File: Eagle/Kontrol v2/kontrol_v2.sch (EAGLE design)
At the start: 21 parts, among them J1 1977477-2, X1 JST-XH-06-PIN-LONG-PAD, X10 JST-XH-02-PIN-LONG-PAD, X11 JST-XH-02-PIN-LONG-PAD, X12 JST-XH-02-PIN-LONG-PAD, X2 JST-XH-06-PIN-LONG-PAD, X3 JST-XH-04-PIN-LONG-PAD, X4 JST-XH-04-PIN-LONG-PAD, X5 JST-XH-04-PIN-LONG-PAD, X6 JST-XH-04-PIN-LONG-PAD, X8 JST-XH-03-PIN-LONG-PAD, X9 JST-XH-02-PIN-LONG-PAD

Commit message: edit kontrol v2
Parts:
- removed X2: JST-XH-06-PIN-LONG-PAD, JST XH Connectors v1-0:JST-XH-06-PIN-LONG-PAD
- removed X4: JST-XH-04-PIN-LONG-PAD, JST XH Connectors v1-0:JST-XH-04-PIN-LONG-PAD
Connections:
- removed net RX_TESTERBOARD: U$1.SD2
- removed net TEMP: X2-5.S
- removed net TX_TESTERBOARD: U$1.SD3
- new net 5V_ESP: U$1.5V
- new net CUR_SENSE: X3-3.S
- new net PWM_DISCHARGE: X1-4.S
- new net PWM_MOSFET: X1-3.S
- new net VOL_SENSE: X3-4.S
- net 12V: no longer X2-1.S
- net 5V: no longer U$1.5V, X2-2.S, X4-1.S
- net CUR_SENSE_1: no longer X3-3.S
- net CUR_SENSE_2: no longer X4-3.S
- net GND: no longer X2-6.S, X4-2.S
- net PWM_DISCHARGE_KANAN: no longer X2-4.S
- net PWM_DISCHARGE_KIRI: no longer X1-4.S
- net PWM_MOSFET_KANAN: no longer X2-3.S
- net PWM_MOSFET_KIRI: no longer X1-3.S
- net VOL_SENSE_1: no longer X3-4.S
- net VOL_SENSE_2: no longer X4-4.S

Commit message: nambahin library eagle+update kontrolv2
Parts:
- removed J1: 1977477-2, terminal_block:1977477-2
- removed JP1: (no value), pinhead:PINHD-1X7
- removed JP5: (no value), pinhead:PINHD-1X10
- added 1K: 1k, rcl:R-US_0204/7
- added 330: 6k, rcl:R-US_0204/7
- added C3: (no value), rcl:CPOL-EUE2,5-6E
- added D4: (no value), Sparkfun_LED:LED5MM
- added D7: UF4007, diode:BAS15
- added JP3: (no value), pinhead:PINHD-1X16
- added JP6: (no value), pinhead:PINHD-1X9
- added JP7: (no value), pinhead:PINHD-1X2
- added JP8: (no value), pinhead:PINHD-1X1
- added K1: SRD-12VDC-SL-C, TA_library:SRD-12VDC-SL-C
- added NPN: (no value), transistor:BC547A-NPN-TO92-CBE
- added U$2: ADS1115, ADS1115:ADS1115
- added U$3: SIM800V2, sim800v2:SIM800V2
- added X2: JST-XH-03-PIN-LONG-PAD, JST XH Connectors v1-0:JST-XH-03-PIN-LONG-PAD
- JP4: device pinhead:PINHD-1X10 -> pinhead:PINHD-1X1
- renumbered X9 to OVR_BMS
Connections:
- removed net CUR_SENSE_1: JP5.7
- removed net CUR_SENSE_2: JP5.9
- removed net N$10: X10-2.S
- removed net N$12: X11-2.S
- removed net N$14: X12-2.S
- removed net N$2: HI_LINK1.AC-, J1.1
- removed net N$3: U$1.IO13
- removed net N$43: JP4.6
- removed net N$46: JP4.9
- removed net N$47: JP4.10
- removed net N$53: JP5.6
- removed net N$7: OVR_BMS-2.S
- removed net PWM_DISCHARGE_KANAN: U$1.IO23
- removed net PWM_DISCHARGE_KIRI: U$1.IO18
- removed net PWM_MOSFET_KANAN: U$1.IO19
- removed net PWM_MOSFET_KIRI: U$1.IO17
- removed net TEMP2: JP4.8
- removed net VOL_SENSE_1: JP5.8
- removed net VOL_SENSE_2: JP5.10
- new net AC: K1.COM
- new net AC_IN_1: K1.NO
- new net EN: C3.+, U$1.EN
- new net N$19: 1K.2, NPN.B
- new net N$21: D7.A, K1.COIL2, NPN.C
- new net N$23: JP3.14, U$1.IO0
- new net N$24: JP3.15, U$1.IO2
- new net N$44: JP8.1, U$2.A3
- new net N$9: JP6.3, U$1.IO12
- new net RELAY: 1K.1, D4.C, JP6.7, U$1.IO25
- new net RX_BMS: JP3.4, U$1.TXD0
- new net RX_IOT: JP6.6, U$1.IO26
- new net TEMP: U$2.A2, X2-2.S
- new net TX_BMS: JP3.5, U$1.RXD0
- new net TX_IOT: JP6.5, U$1.IO27
- net 12V: now also JP4.1
- net 5V: now also D7.C, JP7.1, K1.COIL1, U$2.5V, U$3.5V, X2-1.S; no longer JP1.7, JP4.1, JP5.1, JP5.5
- net 5V_ESP: now also JP7.2
- net BLU_KANAN: now also JP3.9, U$1.IO18; no longer U$1.IO5
- net BLU_KIRI: now also JP3.13, U$1.IO4; no longer U$1.IO0
- net CUR_SENSE: now also U$2.A0
- net DETEKSI_BATERAI_KANAN: now also JP6.8
- net DETEKSI_BATERAI_KIRI: now also JP6.9, U$1.IO32; no longer U$1.IO26
- net GND: now also 330.1, C3.-, JP3.1, JP3.7, NPN.E, OVR_BMS-2.S, U$2.ADDR, U$2.GND, U$3.GND, U$3.GND\, X10-2.S, X11-2.S, X12-2.S, X2-3.S; no longer JP1.6, JP4.2, JP4.5, JP5.2
- net GRN_KANAN: now also JP3.2, U$1.IO23; no longer U$1.IO16
- net GRN_KIRI: now also JP3.11, U$1.IO17; no longer U$1.IO2
- net N$1: now also 330.2, D4.A; no longer HI_LINK1.AC+, J1.2
- net N$8: now also JP6.2, U$1.GND@14; no longer U$1.IO32
- net OVERRIDE_BMS: now also JP6.1, U$1.IO13; no longer U$1.IO27
- net PWM_DISCHARGE: now also JP3.16, U$1.IO15
- net PWM_MOSFET: now also JP3.10, U$1.IO5
- net RED_KANAN: now also JP3.8, U$1.IO19; no longer U$1.IO4
- net RED_KIRI: now also JP3.12, U$1.IO16; no longer U$1.IO15
- net RX: now also U$3.RX; no longer JP1.4, U$1.RXD0
- net SCL: now also JP3.3, U$2.SCL; no longer JP4.3, JP5.3
- net SDA: now also JP3.6, U$2.SDA; no longer JP4.4, JP5.4
- net SWITCH_MODE_DAYA: now also JP6.4, U$1.IO14; no longer U$1.IO25
- net TEMP1: no longer JP4.7
- net TX: now also U$3.TX; no longer JP1.3, U$1.TXD0
- net VOL_SENSE: now also U$2.A1
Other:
- note removed: "RST GND RX TX VDD GND 5V"
- moved on the sheet: X1-1, X1-2, X1-3, X1-4, X1-5, X1-6

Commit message: Update board kontrol
Harusnya sudah selesai
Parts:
- removed X1: JST-XH-06-PIN-LONG-PAD, JST XH Connectors v1-0:JST-XH-06-PIN-LONG-PAD
- removed X5, X6: JST-XH-04-PIN-LONG-PAD, JST XH Connectors v1-0:JST-XH-04-PIN-LONG-PAD
- added 5V: 5V, pinhead:PINHD-1X5
- added C5: 2mF, rcl:CPOL-EUE3.5-10
- added CHARGER: JST-XH-08-PIN-LONG-PAD, Rembrandt Electronics - JST XH Connectors v1-0:JST-XH-08-PIN-LONG-PAD
- added GND: GND, pinhead:PINHD-1X5
- added LED_L, LED_R: JST-XH-04-PIN-LONG-PAD, JST XH Connectors v1-0:JST-XH-04-PIN-LONG-PAD
- added U$4: TERMINAL_4P, TA_library:TERMINAL_4P
- C1: value (none) -> 22u
- C2: value (none) -> 100n
- C3: value (none) -> 4.7uF
- D4: value (none) -> LED_G
- NPN: value (none) -> BS170
- renumbered X10 to CHGMODE, X11 to DB_L, X12 to DB_R, X2 to TEMP, X3 to SENSING, X8 to FAN
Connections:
- removed net AC: K1.COM
- removed net AC_IN_1: K1.NO
- removed net CUR_SENSE: SENSING-3.S, U$2.A0
- removed net N$4: JP2.1
- removed net N$5: JP2.3
- removed net N$6: JP2.5
- removed net RX: U$3.RX
- removed net TEMP: TEMP-2.S, U$2.A2
- removed net TEMP1: X1-5.S
- removed net TX: U$3.TX
- removed net VOL_SENSE: SENSING-4.S, U$2.A1
- new net AC+: HI_LINK1.AC+, U$4.IN_2, U$4.IN_3
- new net AC-: HI_LINK1.AC-, K1.COM, U$4.IN_1
- new net AC_OUT_CHG: K1.NO, U$4.IN_4
- new net CURRENT_SENSE: CHARGER-6.S, SENSING-3.S, U$2.A0
- new net N$2: FAN-1.S
- new net TEMP_SENSE: CHARGER-5.S, TEMP-2.S, U$2.A2
- new net VOLTAGE_SENSE: CHARGER-7.S, SENSING-4.S, U$2.A1
- net 12V: now also CHARGER-1.S; no longer X1-1.S
- net 5V: now also 5V.1, 5V.2, 5V.3, 5V.4, 5V.5, C5.+, CHARGER-2.S; no longer X1-2.S
- net BLU_KANAN: now also LED_R-3.S; no longer X6-2.S
- net BLU_KIRI: now also LED_L-3.S; no longer X5-2.S
- net GND: now also C5.-, CHARGER-8.S, GND.1, GND.2, GND.3, GND.4, GND.5, JP2.5, LED_L-4.S, LED_R-4.S; no longer JP3.1, U$1.GND@38, X1-6.S, X5-1.S, X6-1.S
- net GRN_KANAN: now also LED_R-1.S; no longer X6-4.S
- net GRN_KIRI: now also LED_L-1.S; no longer X5-4.S
- net PWM_DISCHARGE: now also CHARGER-4.S; no longer X1-4.S
- net PWM_MOSFET: now also CHARGER-3.S; no longer X1-3.S
- net RED_KANAN: now also LED_R-2.S; no longer X6-3.S
- net RED_KIRI: now also LED_L-2.S; no longer X5-3.S
- net RX_BMS: now also JP2.1
- net RX_IOT: now also U$3.RX
- net TX_BMS: now also JP2.3
- net TX_IOT: now also U$3.TX
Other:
- moved on the sheet: 1K, 330, D7, JP6, NPN

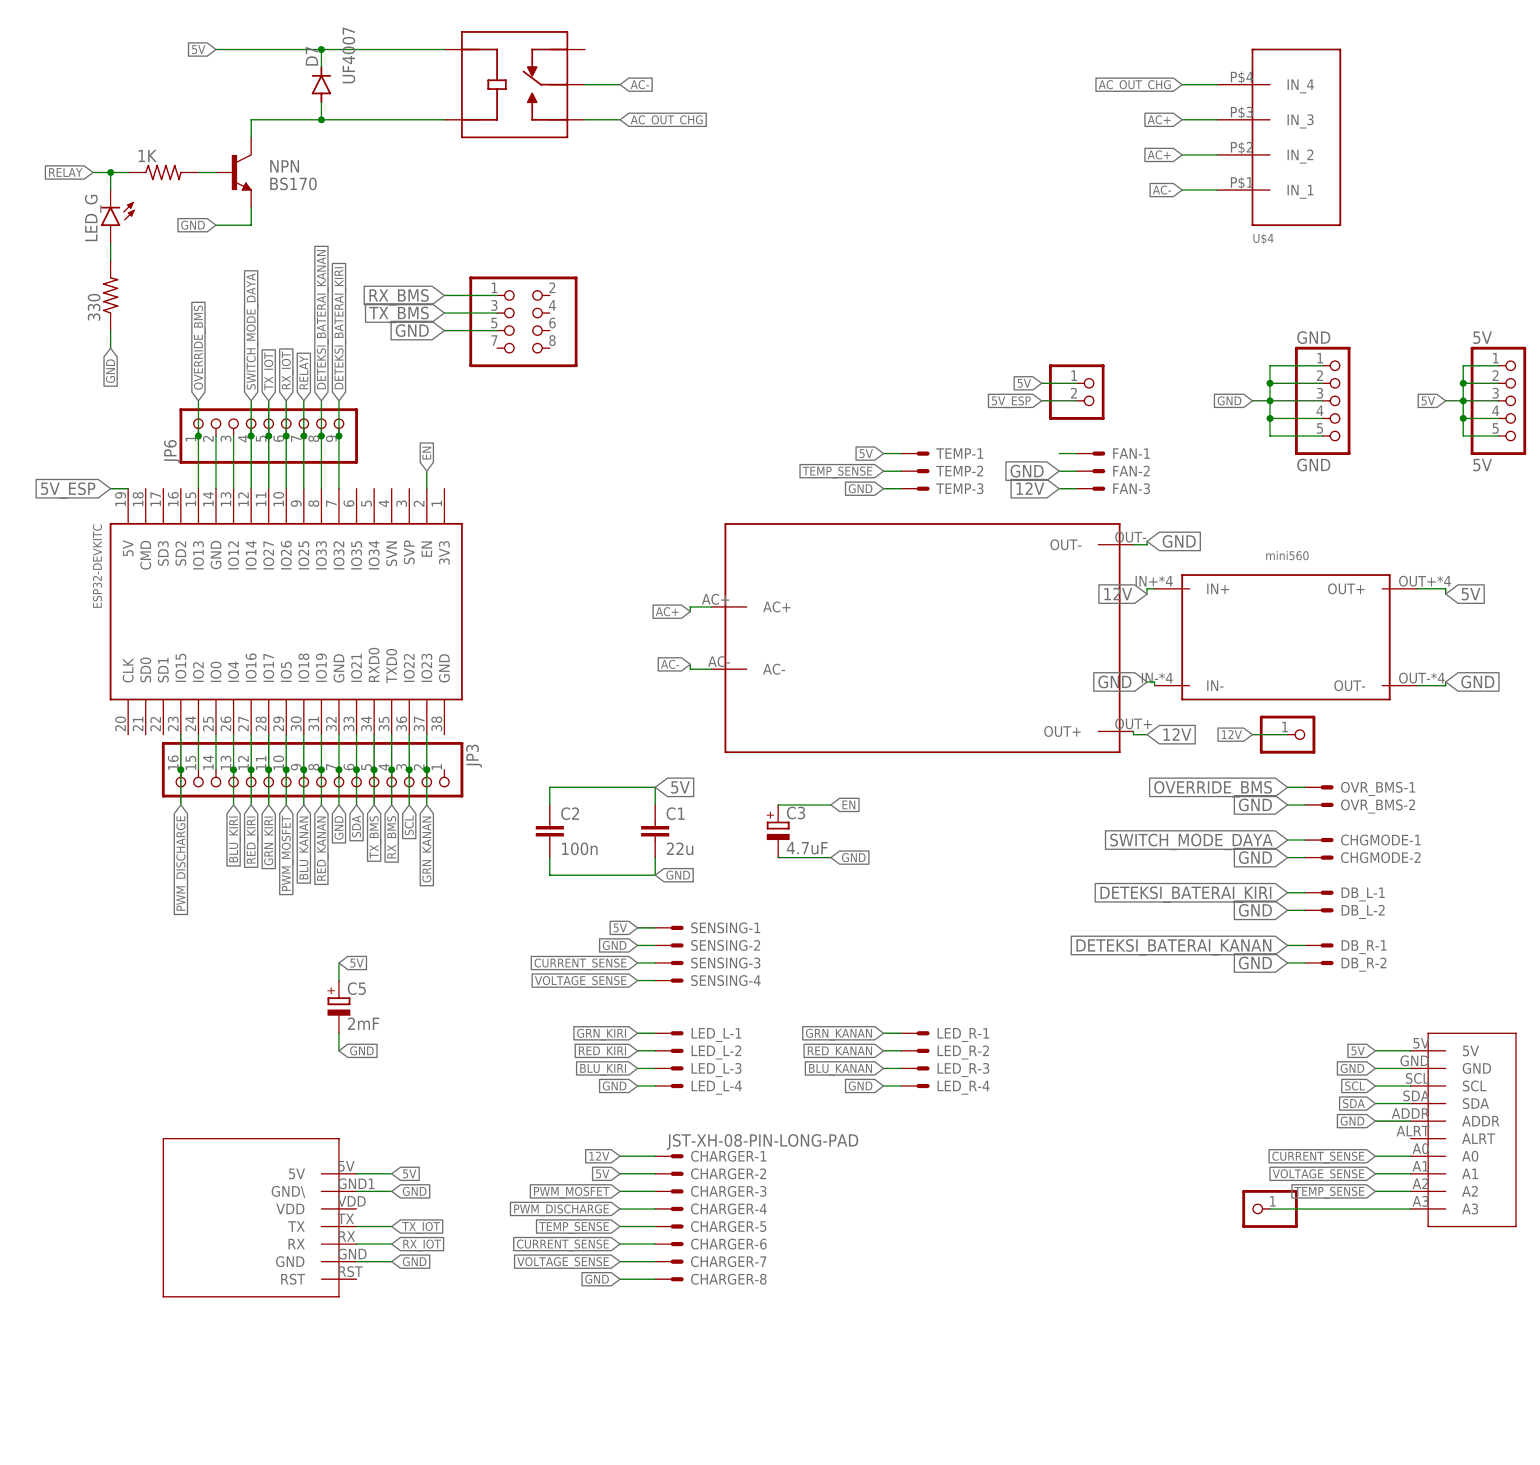
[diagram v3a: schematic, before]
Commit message: Update kontrol
XH8 -> xh10
4p term -> 2p term x2
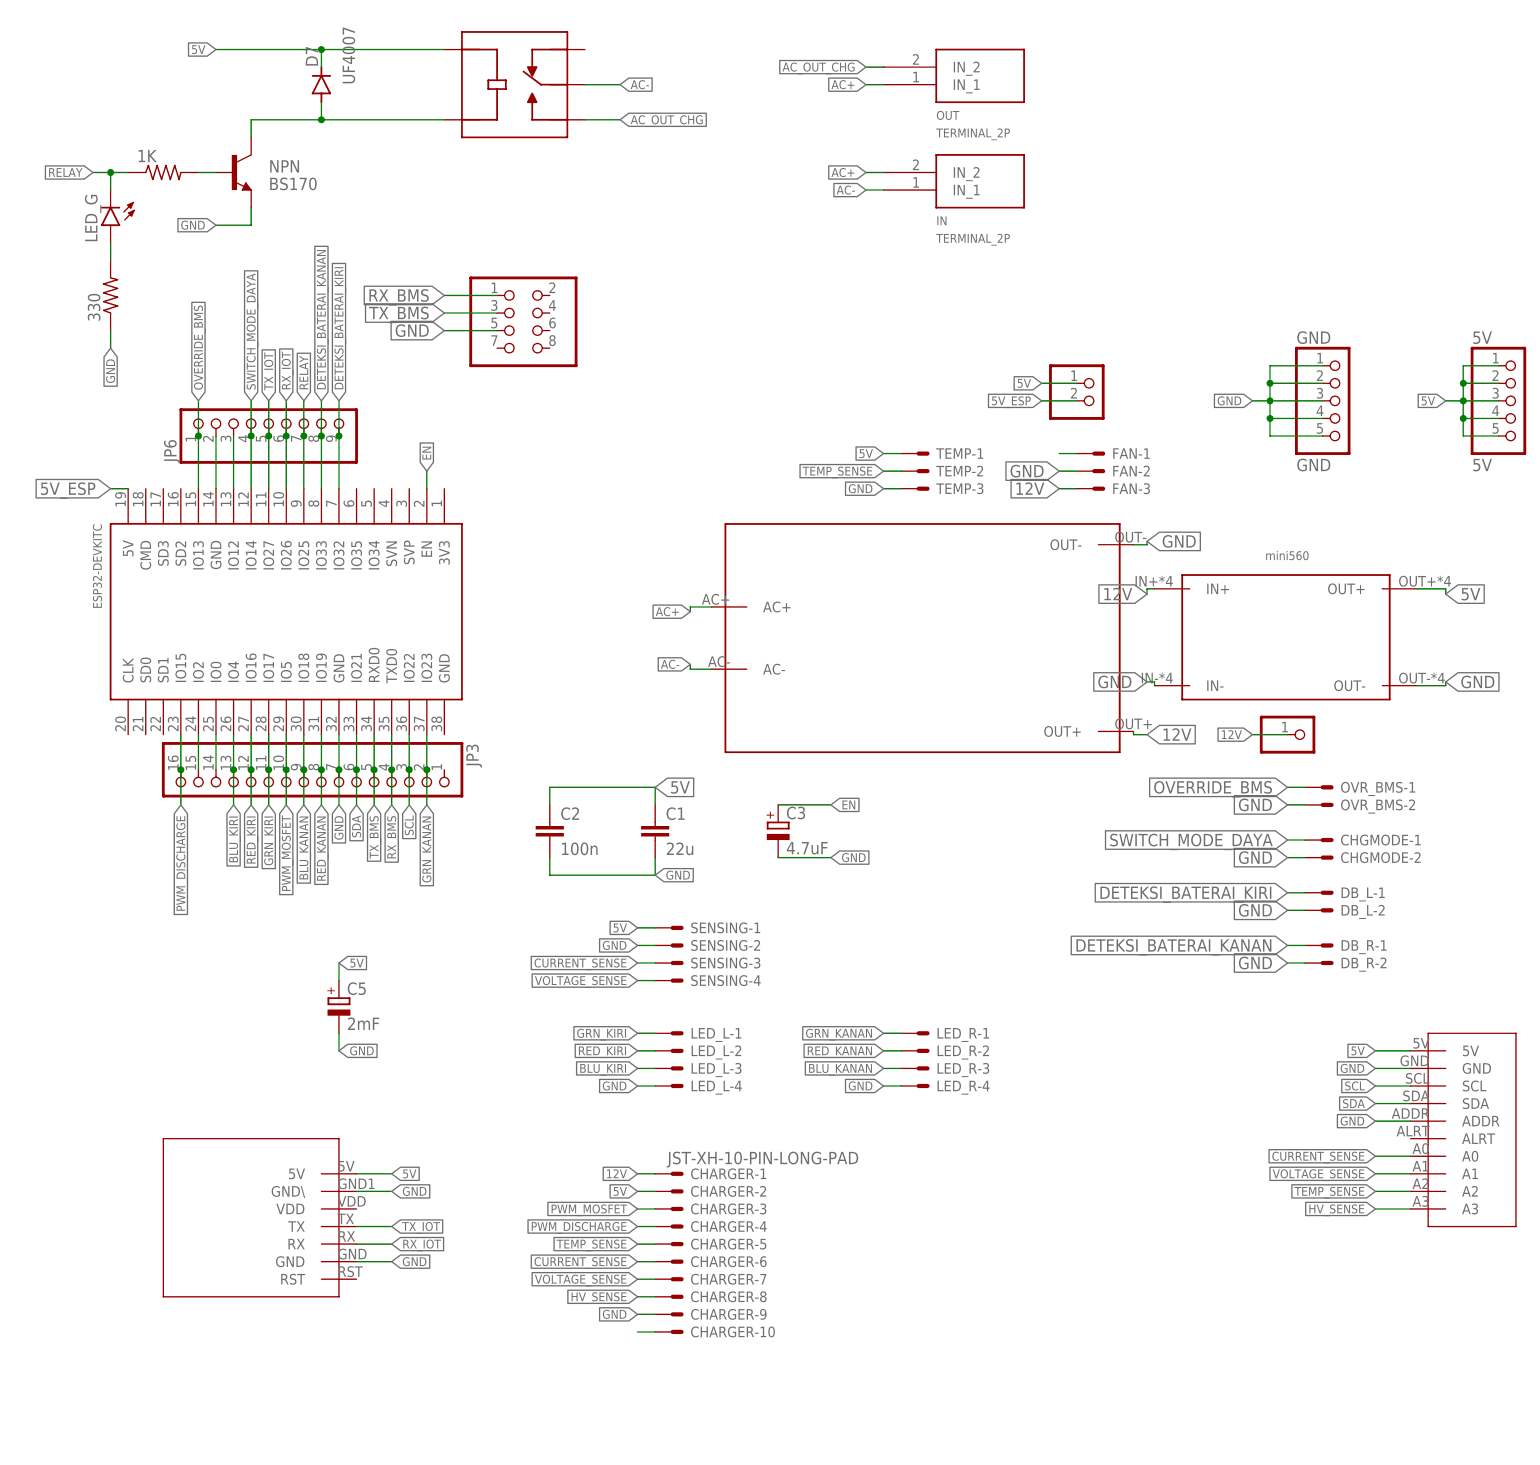
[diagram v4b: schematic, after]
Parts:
- removed JP8: (no value), pinhead:PINHD-1X1
- removed U$4: TERMINAL_4P, TA_library:TERMINAL_4P
- added IN, OUT: TERMINAL_2P, TA_library:TERMINAL_2P
- CHARGER: value JST-XH-08-PIN-LONG-PAD -> JST-XH-10-PIN-LONG-PAD; device Rembrandt Electronics - JST XH Connectors v1-0:JST-XH-08-PIN-LONG-PAD -> Rembrandt Electronics - JST XH Connectors v1-0:JST-XH-10-PIN-LONG-PAD
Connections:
- removed net N$44: JP8.1, U$2.A3
- new net HV_SENSE: CHARGER-8.S, U$2.A3
- new net N$14: CHARGER-10.S
- net AC+: now also IN.IN_2, OUT.IN_1; no longer U$4.IN_2, U$4.IN_3
- net AC-: now also IN.IN_1; no longer U$4.IN_1
- net AC_OUT_CHG: now also OUT.IN_2; no longer U$4.IN_4
- net GND: now also CHARGER-9.S; no longer CHARGER-8.S
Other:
- moved on the sheet: CHARGER-1, CHARGER-2, CHARGER-3, CHARGER-4, CHARGER-5, CHARGER-6, CHARGER-7, CHARGER-8

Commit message: update kontrol
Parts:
- renumbered 330 to R2
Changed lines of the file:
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@@
 <part name="U$3" library="sim800v2" deviceset="SIM800V2" device=""/>
 <part name="D4" library="Sparkfun_LED" deviceset="LED" device="5MM" value="LED_G"/>
-<part name="330" library="rcl" library_urn="urn:adsk.eagle:library:334" deviceset="R-US_" device="0204/7" package3d_urn="urn:adsk.eagle:package:23498/2" value="6k"/>
+<part name="R2" library="rcl" library_urn="urn:adsk.eagle:library:334" deviceset="R-US_" device="0204/7" package3d_urn="urn:adsk.eagle:package:23498/2" value="6k"/>
 <part name="GND" library="pinhead" library_urn="urn:adsk.eagle:library:325" deviceset="PINHD-1X5" device="" package3d_urn="urn:adsk.eagle:package:22469/2" value="GND"/>
 <part name="5V" library="pinhead" library_urn="urn:adsk.eagle:library:325" deviceset="PINHD-1X5" device="" package3d_urn="urn:adsk.eagle:package:22469/2" value="5V"/>
@@
 <attribute name="VALUE" x="-207.645" y="212.852" size="1.778" layer="96" font="vector" rot="R270" align="top-left"/>
 </instance>
-<instance part="330" gate="G$1" x="-205.74" y="198.12" smashed="yes" rot="R90">
+<instance part="R2" gate="G$1" x="-205.74" y="198.12" smashed="yes" rot="R90">
 <attribute name="NAME" x="-207.2386" y="194.31" size="1.778" layer="95" rot="R90"/>
 </instance>
@@
 </segment>
 <segment>
-<pinref part="330" gate="G$1" pin="1"/>
+<pinref part="R2" gate="G$1" pin="1"/>
 <wire x1="-205.74" y1="193.04" x2="-205.74" y2="190.5" width="0.1524" layer="91"/>
 <label x="-205.74" y="190.5" size="1.27" layer="95" rot="R270" xref="yes"/>
@@
 <segment>
 <pinref part="D4" gate="D1" pin="A"/>
-<pinref part="330" gate="G$1" pin="2"/>
+<pinref part="R2" gate="G$1" pin="2"/>
 <wire x1="-205.74" y1="205.74" x2="-205.74" y2="203.2" width="0.1524" layer="91"/>
 </segment>

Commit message: update kontrol
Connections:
- net N$1: now also D4.C; no longer D4.A
- net RELAY: now also D4.A; no longer D4.C
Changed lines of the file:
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@@
 </instance>
 <instance part="U$3" gate="G$1" x="-177.8" y="63.5" smashed="yes"/>
-<instance part="D4" gate="D1" x="-205.74" y="208.28" smashed="yes" rot="R180">
-<attribute name="VALUE" x="-207.645" y="212.852" size="1.778" layer="96" font="vector" rot="R270" align="top-left"/>
+<instance part="D4" gate="D1" x="-205.74" y="210.82" smashed="yes">
+<attribute name="VALUE" x="-203.835" y="206.248" size="1.778" layer="96" font="vector" rot="R90" align="top-left"/>
 </instance>
 <instance part="R2" gate="G$1" x="-205.74" y="198.12" smashed="yes" rot="R90">
@@
 <segment>
 <pinref part="1K" gate="G$1" pin="1"/>
+<label x="-208.28" y="215.9" size="1.27" layer="95" rot="R180" xref="yes"/>
 <wire x1="-203.2" y1="215.9" x2="-205.74" y2="215.9" width="0.1524" layer="91"/>
-<label x="-208.28" y="215.9" size="1.27" layer="95" rot="R180" xref="yes"/>
-<pinref part="D4" gate="D1" pin="C"/>
+<pinref part="D4" gate="D1" pin="A"/>
 <wire x1="-205.74" y1="215.9" x2="-208.28" y2="215.9" width="0.1524" layer="91"/>
-<wire x1="-205.74" y1="213.36" x2="-205.74" y2="215.9" width="0.1524" layer="91"/>
-<junction x="-205.74" y="215.9"/>
+<wire x1="-205.74" y1="215.9" x2="-205.74" y2="213.36" width="0.1524" layer="91"/>
 </segment>
 <segment>
@@
 </segment>
 </net>
-<net name="N$1" class="0">
-<segment>
-<pinref part="D4" gate="D1" pin="A"/>
-<pinref part="R2" gate="G$1" pin="2"/>
-<wire x1="-205.74" y1="205.74" x2="-205.74" y2="203.2" width="0.1524" layer="91"/>
-</segment>
-</net>
 <net name="TEMP_SENSE" class="0">
 <segment>
@@
 </segment>
 </net>
+<net name="N$1" class="0">
+<segment>
+<pinref part="D4" gate="D1" pin="C"/>
+<pinref part="R2" gate="G$1" pin="2"/>
+<wire x1="-205.74" y1="205.74" x2="-205.74" y2="203.2" width="0.1524" layer="91"/>
+</segment>
+</net>
